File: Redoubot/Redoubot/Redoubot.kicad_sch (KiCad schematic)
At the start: 33 parts, among them J1 Connecteur batterie, J2 Moteur 1, J3 Moteur 2, J4 TOF, J5 MPU-6050, J6 ADA3595, U1 STM32G431RBTx, U2 DRV8833PWP, U3 BQ25896RTWR

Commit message: added the crystal and some missing connections
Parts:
- added R11: R, symbol Device:R
- added Y1: Crystal, symbol Device:Crystal
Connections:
- net 3V3: now also R11.1
- net GND: no longer J5.7 (Pin_7)
- net PWMN MOT1: now reaches U1.18 (PA4)
- net PWMN MOT1: now also U2.15 (AIN2)
- net PWMN MOT2: now reaches U1.20 (PA6)
- net PWMN MOT2: now also U2.10 (BIN2)
- net at U2.1 (~{SLEEP}): now also R11.2
- no-connect marks 7 -> 8
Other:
- moved on the sheet: C10, C8, C9, R9, U2

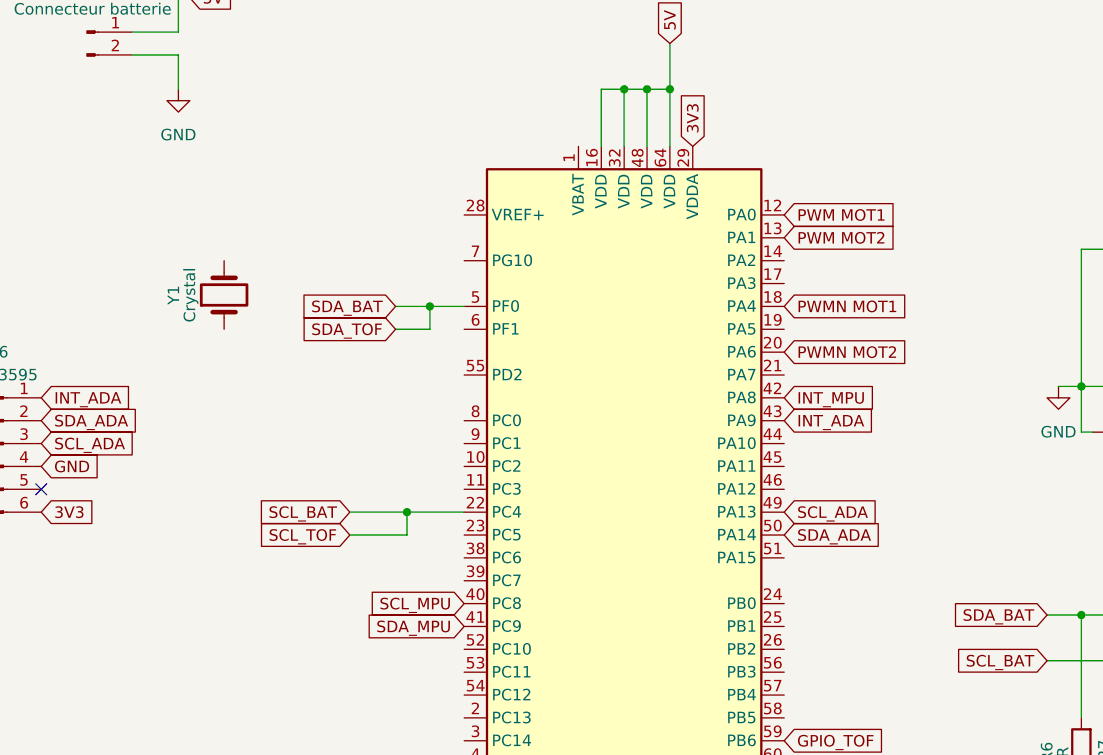
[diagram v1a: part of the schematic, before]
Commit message: connected the crystal to the STM32
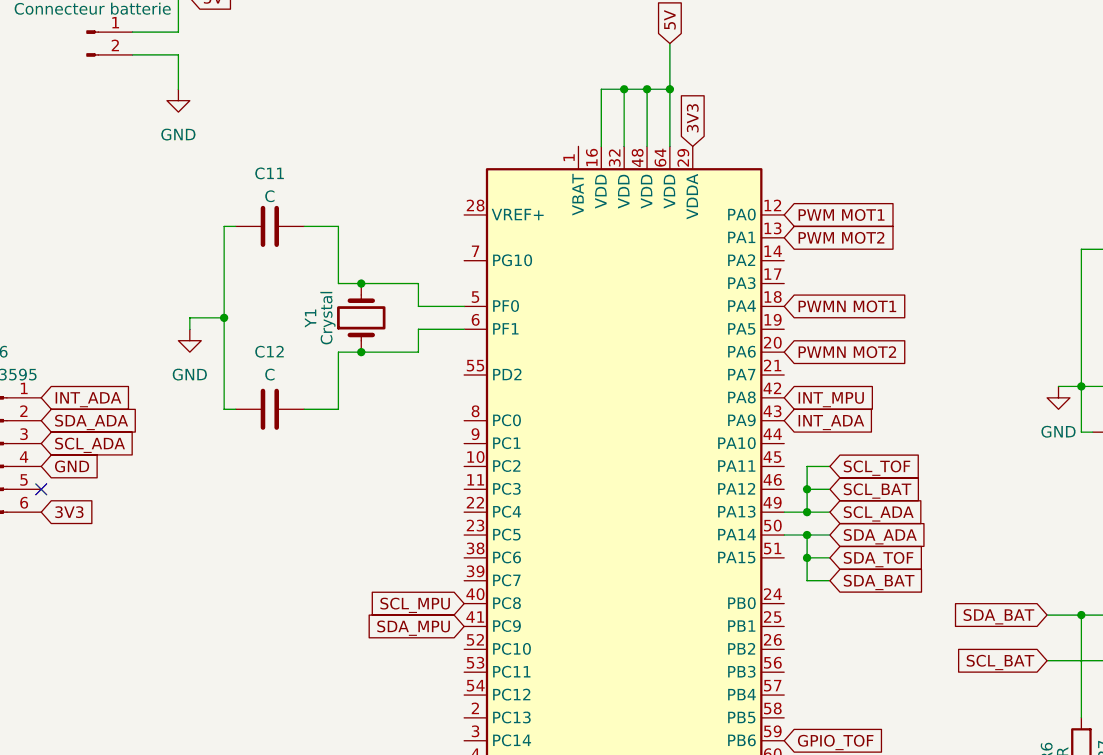
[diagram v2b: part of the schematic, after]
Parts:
- added C11, C12: C, symbol Device:C
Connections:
- net GND: now also C11.1, C12.1
- net SCL_ADA: now also J4.3 (Pin_3), R7.2, U3.5 (SCL)
- net SDA_ADA: now also J4.4 (Pin_4), R6.2, U3.6 (SDA)
- net at U1.6 (PF1): now also Y1.1, C12.2
- net at Y1.2: now also U1.5 (PF0), C11.2
- removed net SCL_BAT: J4.3 (Pin_3), R7.2, U1.22 (PC4), U3.5 (SCL)
- removed net SDA_BAT: J4.4 (Pin_4), R6.2, U1.5 (PF0), U3.6 (SDA)
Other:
- moved on the sheet: Y1

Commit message: Added numerical values of the crystal and the associated capacitors
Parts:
- C11, C12: value C -> 33p
- Y1: value Crystal -> 8MHz
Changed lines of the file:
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@@
 			)
 		)
-		(property "Value" "C"
+		(property "Value" "33p"
 			(at 81.28 59.69 90)
 			(show_name no)
@@
 			)
 		)
-		(property "Value" "Crystal"
+		(property "Value" "8MHz"
 			(at 87.63 53.34 0)
 			(show_name no)
@@
 			)
 		)
-		(property "Value" "C"
+		(property "Value" "33p"
 			(at 81.28 39.878 90)
 			(show_name no)
